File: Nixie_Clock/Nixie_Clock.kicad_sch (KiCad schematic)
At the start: 0 parts

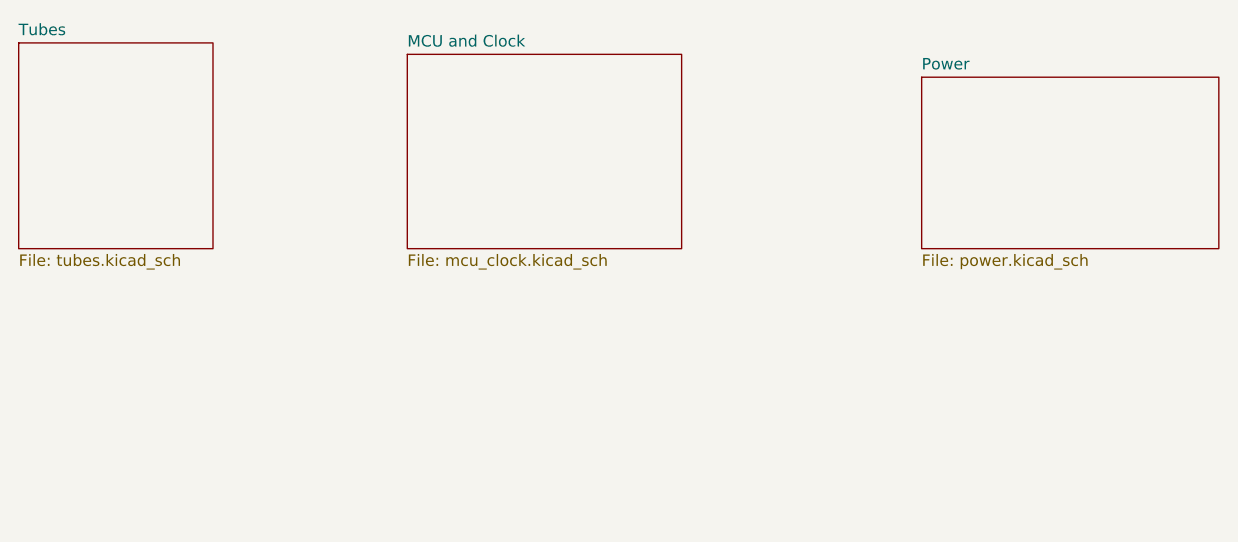
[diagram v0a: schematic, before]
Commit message: Complete prelim nixie driver. Begin MCU work.
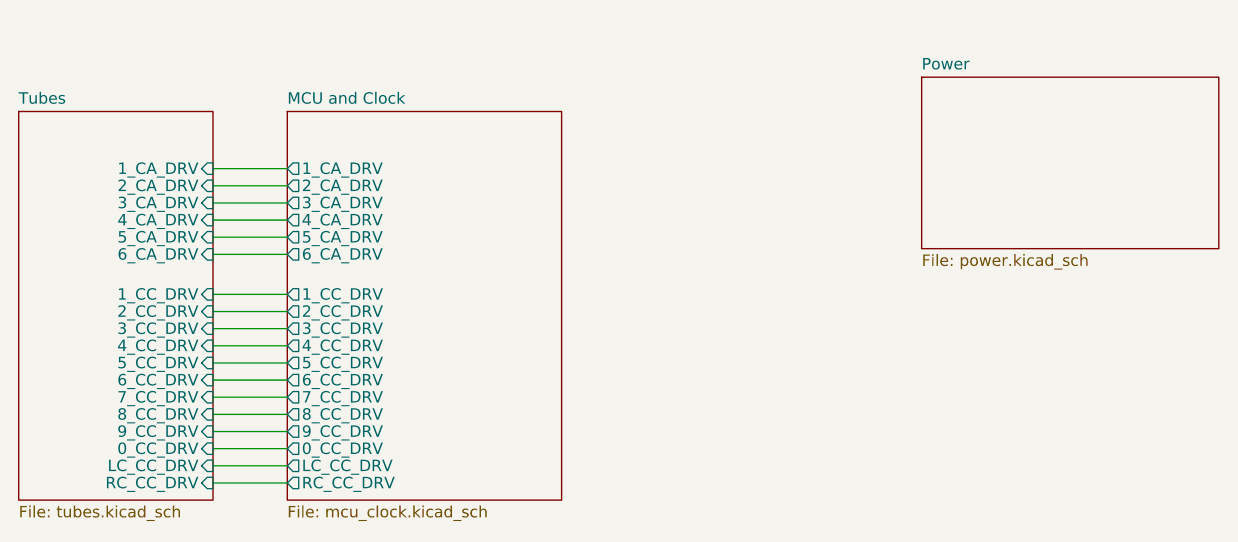
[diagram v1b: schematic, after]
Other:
- sheet MCU and Clock ports: added 0_CC_DRV, 1_CA_DRV, 1_CC_DRV, 2_CA_DRV, 2_CC_DRV, 3_CA_DRV, 3_CC_DRV, 4_CA_DRV, 4_CC_DRV, 5_CA_DRV, 5_CC_DRV, 6_CA_DRV, 6_CC_DRV, 7_CC_DRV, 8_CC_DRV, 9_CC_DRV, LC_CC_DRV, RC_CC_DRV; removed none
- sheet Tubes ports: added 0_CC_DRV, 1_CA_DRV, 1_CC_DRV, 2_CA_DRV, 2_CC_DRV, 3_CA_DRV, 3_CC_DRV, 4_CA_DRV, 4_CC_DRV, 5_CA_DRV, 5_CC_DRV, 6_CA_DRV, 6_CC_DRV, 7_CC_DRV, 8_CC_DRV, 9_CC_DRV, LC_CC_DRV, RC_CC_DRV; removed none
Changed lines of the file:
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@@
 (kicad_sch (version 20230121) (generator eeschema)
-  (paper "A4")
+  (paper "USLedger")
+  (wire (pts (xy 76.2 62.865) (xy 84.455 62.865))
+    (stroke (width 0) (type default))
+  )
+  (wire (pts (xy 76.2 64.77) (xy 84.455 64.77))
+    (stroke (width 0) (type default))
+  )
+  (wire (pts (xy 76.2 68.58) (xy 84.455 68.58))
+    (stroke (width 0) (type default))
+  )
+  (wire (pts (xy 76.2 60.96) (xy 84.455 60.96))
+    (stroke (width 0) (type default))
+  )
+  (wire (pts (xy 76.2 74.295) (xy 84.455 74.295))
+    (stroke (width 0) (type default))
+  )
+  (wire (pts (xy 76.2 78.105) (xy 84.455 78.105))
+    (stroke (width 0) (type default))
+  )
+  (wire (pts (xy 76.2 81.915) (xy 84.455 81.915))
+    (stroke (width 0) (type default))
+  )
+  (wire (pts (xy 76.2 80.01) (xy 84.455 80.01))
+    (stroke (width 0) (type default))
+  )
+  (wire (pts (xy 76.2 66.675) (xy 84.455 66.675))
+    (stroke (width 0) (type default))
+  )
+  (wire (pts (xy 76.2 48.895) (xy 84.455 48.895))
+    (stroke (width 0) (type default))
+  )
+  (wire (pts (xy 76.2 50.8) (xy 84.455 50.8))
+    (stroke (width 0) (type default))
+  )
+  (wire (pts (xy 76.2 76.2) (xy 84.455 76.2))
+    (stroke (width 0) (type default))
+  )
+  (wire (pts (xy 76.2 72.39) (xy 84.455 72.39))
+    (stroke (width 0) (type default))
+  )
+  (wire (pts (xy 76.2 56.515) (xy 84.455 56.515))
+    (stroke (width 0) (type default))
+  )
+  (wire (pts (xy 76.2 54.61) (xy 84.455 54.61))
+    (stroke (width 0) (type default))
+  )
+  (wire (pts (xy 76.2 70.485) (xy 84.455 70.485))
+    (stroke (width 0) (type default))
+  )
+  (wire (pts (xy 76.2 46.99) (xy 84.455 46.99))
+    (stroke (width 0) (type default))
+  )
+  (wire (pts (xy 76.2 52.705) (xy 84.455 52.705))
+    (stroke (width 0) (type default))
+  )
   (sheet (at 154.94 36.83) (size 33.02 19.05) (fields_autoplaced)
     (stroke (width 0.1524) (type solid))
@@
     )
   )
-  (sheet (at 97.79 34.29) (size 30.48 21.59) (fields_autoplaced)
+  (sheet (at 84.455 40.64) (size 30.48 43.18) (fields_autoplaced)
     (stroke (width 0.1524) (type solid))
     (fill (color 0 0 0 0.0000))
-    (property "Sheetname" "MCU and Clock" (at 97.79 33.5784 0)
+    (property "Sheetname" "MCU and Clock" (at 84.455 39.9284 0)
       (effects (font (size 1.27 1.27)) (justify left bottom))
     )
-    (property "Sheetfile" "mcu_clock.kicad_sch" (at 97.79 56.4646 0)
+    (property "Sheetfile" "mcu_clock.kicad_sch" (at 84.455 84.4046 0)
       (effects (font (size 1.27 1.27)) (justify left top))
+    )
+    (pin "4_CC_DRV" output (at 84.455 66.675 180)
+      (effects (font (size 1.27 1.27)) (justify left))
+    )
+    (pin "3_CC_DRV" output (at 84.455 64.77 180)
+      (effects (font (size 1.27 1.27)) (justify left))
+    )
+    (pin "5_CC_DRV" output (at 84.455 68.58 180)
+      (effects (font (size 1.27 1.27)) (justify left))
+    )
+    (pin "6_CC_DRV" output (at 84.455 70.485 180)
+      (effects (font (size 1.27 1.27)) (justify left))
+    )
+    (pin "2_CC_DRV" output (at 84.455 62.865 180)
+      (effects (font (size 1.27 1.27)) (justify left))
+    )
+    (pin "1_CC_DRV" output (at 84.455 60.96 180)
+      (effects (font (size 1.27 1.27)) (justify left))
+    )
+    (pin "7_CC_DRV" output (at 84.455 72.39 180)
+      (effects (font (size 1.27 1.27)) (justify left))
+    )
+    (pin "8_CC_DRV" output (at 84.455 74.295 180)
+      (effects (font (size 1.27 1.27)) (justify left))
+    )
+    (pin "9_CC_DRV" output (at 84.455 76.2 180)
+      (effects (font (size 1.27 1.27)) (justify left))
+    )
+    (pin "0_CC_DRV" output (at 84.455 78.105 180)
+      (effects (font (size 1.27 1.27)) (justify left))
+    )
+    (pin "LC_CC_DRV" output (at 84.455 80.01 180)
+      (effects (font (size 1.27 1.27)) (justify left))
+    )
+    (pin "RC_CC_DRV" output (at 84.455 81.915 180)
+      (effects (font (size 1.27 1.27)) (justify left))
+    )
+    (pin "4_CA_DRV" output (at 84.455 52.705 180)
+      (effects (font (size 1.27 1.27)) (justify left))
+    )
+    (pin "3_CA_DRV" output (at 84.455 50.8 180)
+      (effects (font (size 1.27 1.27)) (justify left))
+    )
+    (pin "1_CA_DRV" output (at 84.455 46.99 180)
+      (effects (font (size 1.27 1.27)) (justify left))
+    )
+    (pin "2_CA_DRV" output (at 84.455 48.895 180)
+      (effects (font (size 1.27 1.27)) (justify left))
+    )
+    (pin "5_CA_DRV" output (at 84.455 54.61 180)
+      (effects (font (size 1.27 1.27)) (justify left))
+    )
+    (pin "6_CA_DRV" output (at 84.455 56.515 180)
+      (effects (font (size 1.27 1.27)) (justify left))
     )
     (instances
@@
     )
   )
-  (sheet (at 54.61 33.02) (size 21.59 22.86) (fields_autoplaced)
+  (sheet (at 54.61 40.64) (size 21.59 43.18) (fields_autoplaced)
     (stroke (width 0.1524) (type solid))
     (fill (color 0 0 0 0.0000))
-    (property "Sheetname" "Tubes" (at 54.61 32.3084 0)
+    (property "Sheetname" "Tubes" (at 54.61 39.9284 0)
       (effects (font (size 1.27 1.27)) (justify left bottom))
     )
-    (property "Sheetfile" "tubes.kicad_sch" (at 54.61 56.4646 0)
+    (property "Sheetfile" "tubes.kicad_sch" (at 54.61 84.4046 0)
       (effects (font (size 1.27 1.27)) (justify left top))
     )
+    (pin "9_CC_DRV" input (at 76.2 76.2 0)
+      (effects (font (size 1.27 1.27)) (justify right))
+    )
+    (pin "0_CC_DRV" input (at 76.2 78.105 0)
+      (effects (font (size 1.27 1.27)) (justify right))
+    )
+    (pin "3_CC_DRV" input (at 76.2 64.77 0)
+      (effects (font (size 1.27 1.27)) (justify right))
+    )
+    (pin "7_CC_DRV" input (at 76.2 72.39 0)
+      (effects (font (size 1.27 1.27)) (justify right))
+    )
+    (pin "8_CC_DRV" input (at 76.2 74.295 0)
+      (effects (font (size 1.27 1.27)) (justify right))
+    )
+    (pin "1_CC_DRV" input (at 76.2 60.96 0)
+      (effects (font (size 1.27 1.27)) (justify right))
+    )
+    (pin "2_CC_DRV" input (at 76.2 62.865 0)
+      (effects (font (size 1.27 1.27)) (justify right))
+    )
+    (pin "5_CC_DRV" input (at 76.2 68.58 0)
+      (effects (font (size 1.27 1.27)) (justify right))
+    )
+    (pin "6_CC_DRV" input (at 76.2 70.485 0)
+      (effects (font (size 1.27 1.27)) (justify right))
+    )
+    (pin "RC_CC_DRV" input (at 76.2 81.915 0)
+      (effects (font (size 1.27 1.27)) (justify right))
+    )
+    (pin "4_CC_DRV" input (at 76.2 66.675 0)
+      (effects (font (size 1.27 1.27)) (justify right))
+    )
+    (pin "LC_CC_DRV" input (at 76.2 80.01 0)
+      (effects (font (size 1.27 1.27)) (justify right))
+    )
+    (pin "3_CA_DRV" input (at 76.2 50.8 0)
+      (effects (font (size 1.27 1.27)) (justify right))
+    )
+    (pin "1_CA_DRV" input (at 76.2 46.99 0)
+      (effects (font (size 1.27 1.27)) (justify right))
+    )
+    (pin "2_CA_DRV" input (at 76.2 48.895 0)
+      (effects (font (size 1.27 1.27)) (justify right))
+    )
+    (pin "4_CA_DRV" input (at 76.2 52.705 0)
+      (effects (font (size 1.27 1.27)) (justify right))
+    )
+    (pin "5_CA_DRV" input (at 76.2 54.61 0)
+      (effects (font (size 1.27 1.27)) (justify right))
+    )
+    (pin "6_CA_DRV" input (at 76.2 56.515 0)
+      (effects (font (size 1.27 1.27)) (justify right))
+    )
     (instances
